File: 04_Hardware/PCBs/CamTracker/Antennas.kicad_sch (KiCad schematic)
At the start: 22 parts, among them J15 636101112001, J16 636101112001, J17 636101112001, J18 636101112001, U1 SC206EEMDA-G51-UGNDA

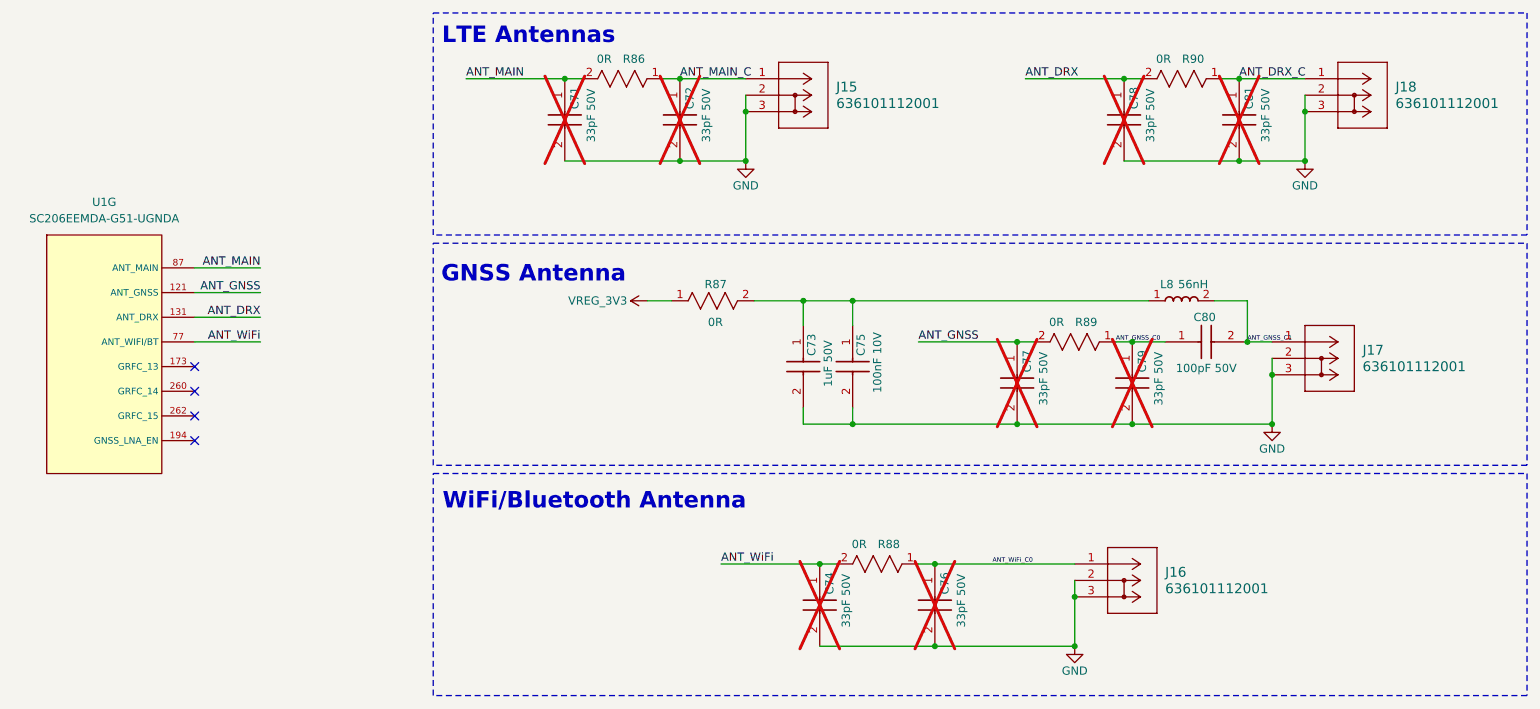
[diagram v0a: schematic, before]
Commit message: feat: Completed Placement v1 in Layout
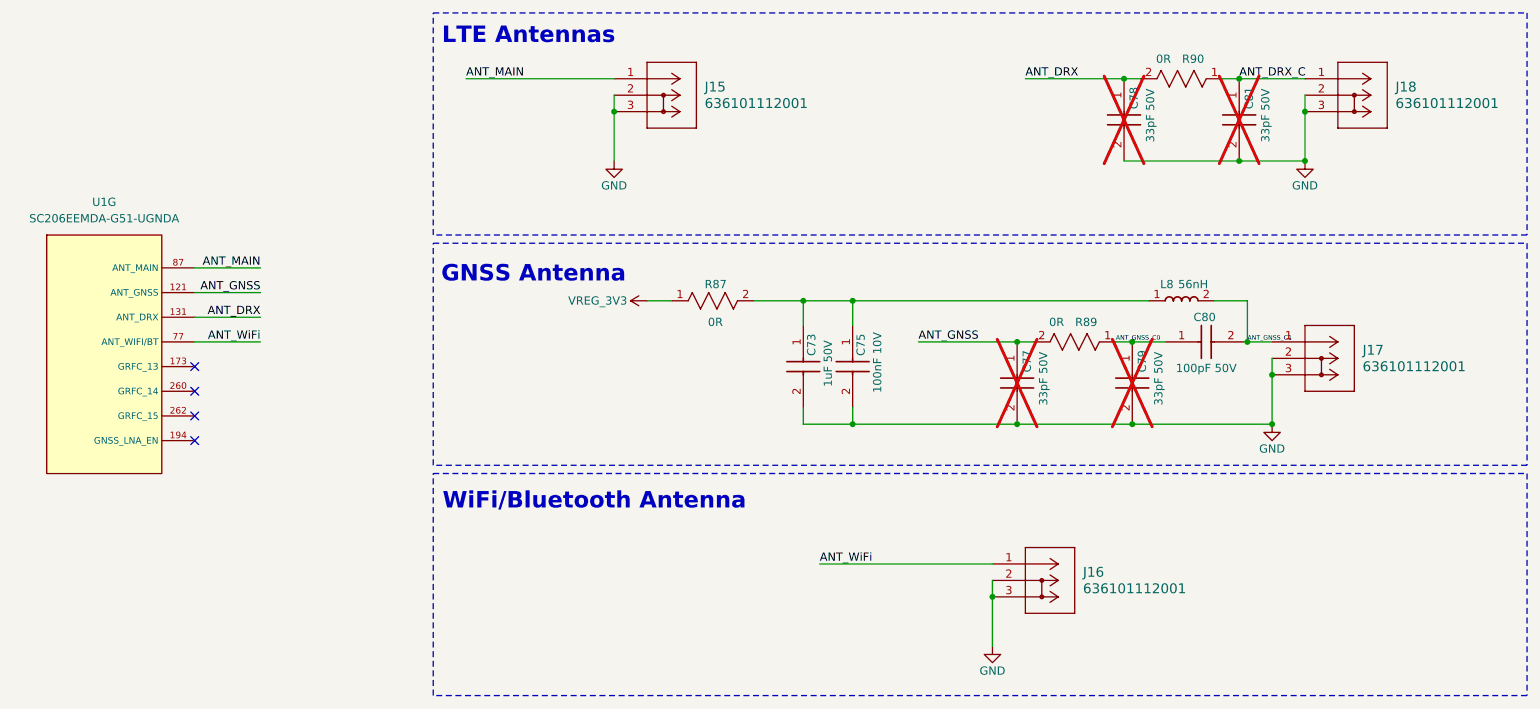
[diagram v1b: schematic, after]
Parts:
- removed C71, C72, C74, C76: 33pF 50V, 000MCLib:CAPC1005X55N, symbol 000MCLib:GRM1555C1H330JA01D
- removed R86, R88: 0R, 000MCLib:RC0402N_YAG, symbol 000MCLib:RC0402JR-070RL
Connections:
- net ANT_MAIN_C is gone; now on net ANT_MAIN: J15.1 (SIGNAL)
- net ANT_WiFi_C0 is gone; now on net ANT_WiFi: J16.1 (SIGNAL)
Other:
- moved on the sheet: J15, J16

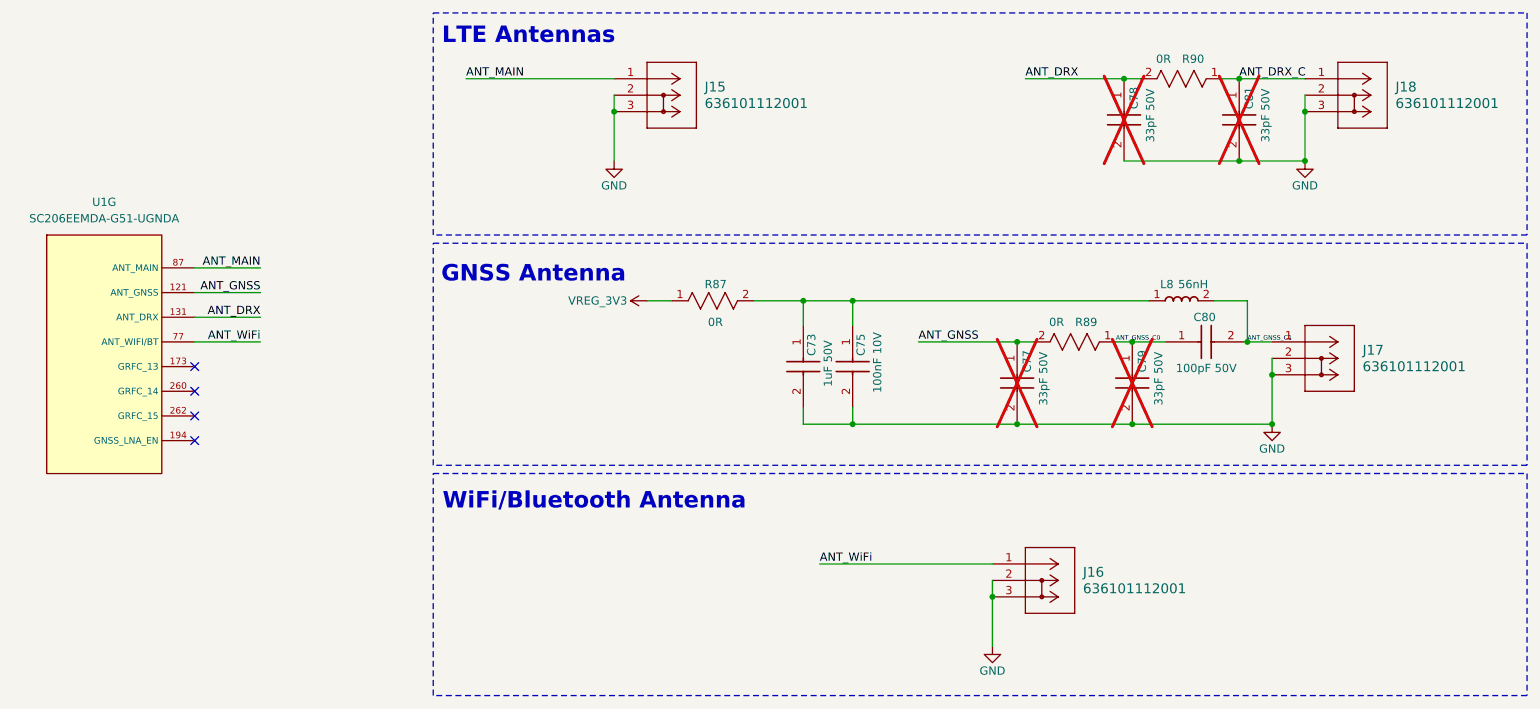
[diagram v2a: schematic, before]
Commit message: feat(PCB): Added TE Connectivity connectors except the SD connector
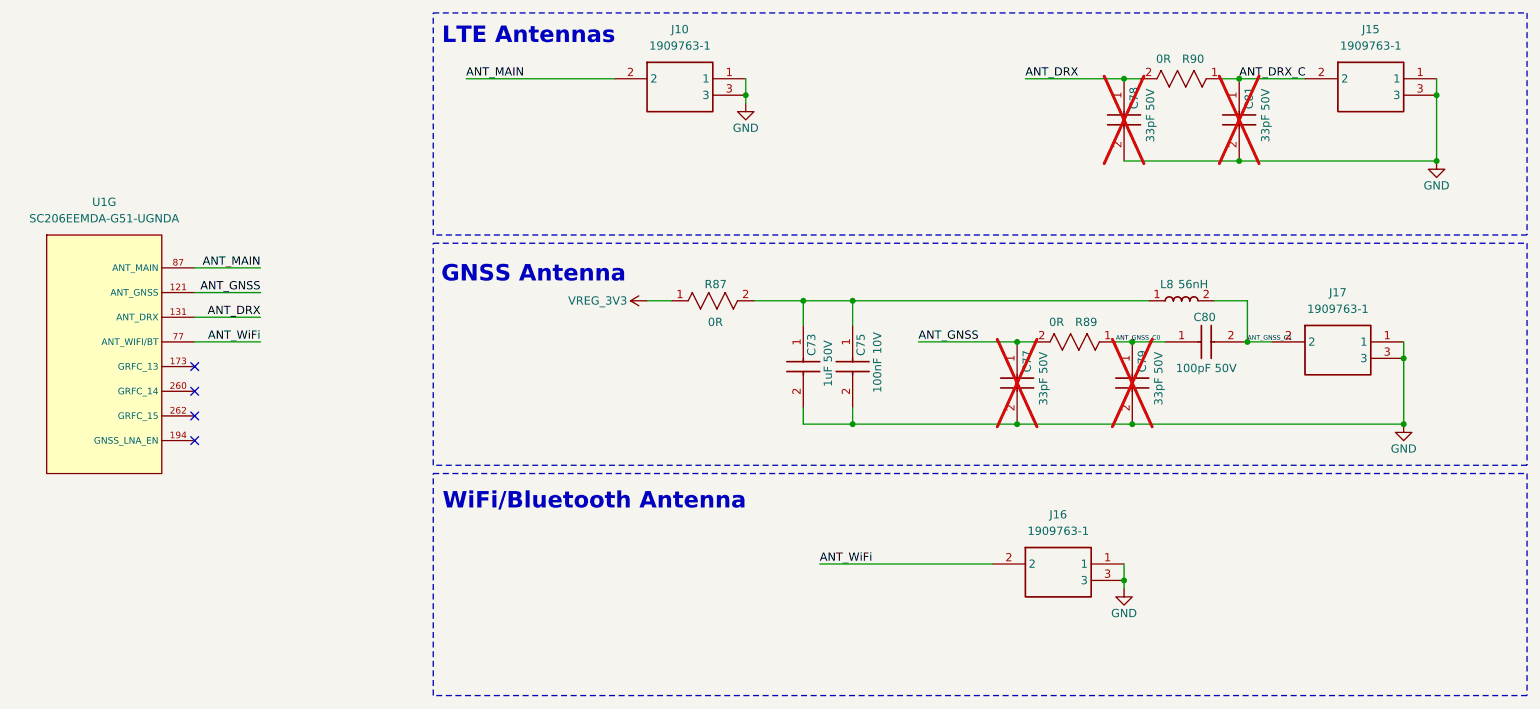
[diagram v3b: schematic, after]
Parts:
- removed J15, J16, J17, J18: 636101112001, 000MCLib:COAX2_636101112001_WRE, symbol 000MCLib:636101112001
- added J10, J15, J16, J17: 1909763-1, 000MCLib:1909763-1, symbol 000MCLib:1909763-1
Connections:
- net ANT_DRX_C: now also J15.2
- net ANT_GNSS_C1: now also J17.2
- net ANT_MAIN: now also J10.2
- net ANT_WiFi: now also J16.2
- net GND: now also J10.1, J10.3, J15.1, J15.3, J16.1, J16.3, J17.1, J17.3

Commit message: feat(PCB): finalize PCB design and generate BOM/Gerbers
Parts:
- R87: Height 0.5 -> (none); Mouser Part Number 71-CRCW0805-0-E3 -> (none); Mouser Price/Stock https://www.mouser.co.uk/ProductDetail/Vishay-Dale/CRCW0805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 -> (none)
